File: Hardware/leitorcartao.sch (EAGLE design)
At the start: 160 parts, among them IC1 TL084, IC2 TL084, Q1 DMN3404, Q4 BC847ALT1SMD, Q5 BC847ALT1SMD, Q6 BC847ALT1SMD, Q7 BC847ALT1SMD, Q8 MMBT4403, Q9 MMBT4401, U1 SAMD20E14A-AUT, U3 TLV1117-50CDCYR, U4 MFRC52202HN1, U5 LP2985-33DBVR, X1 MIFARE, X3 ANTENA, Y1 27.12MHz

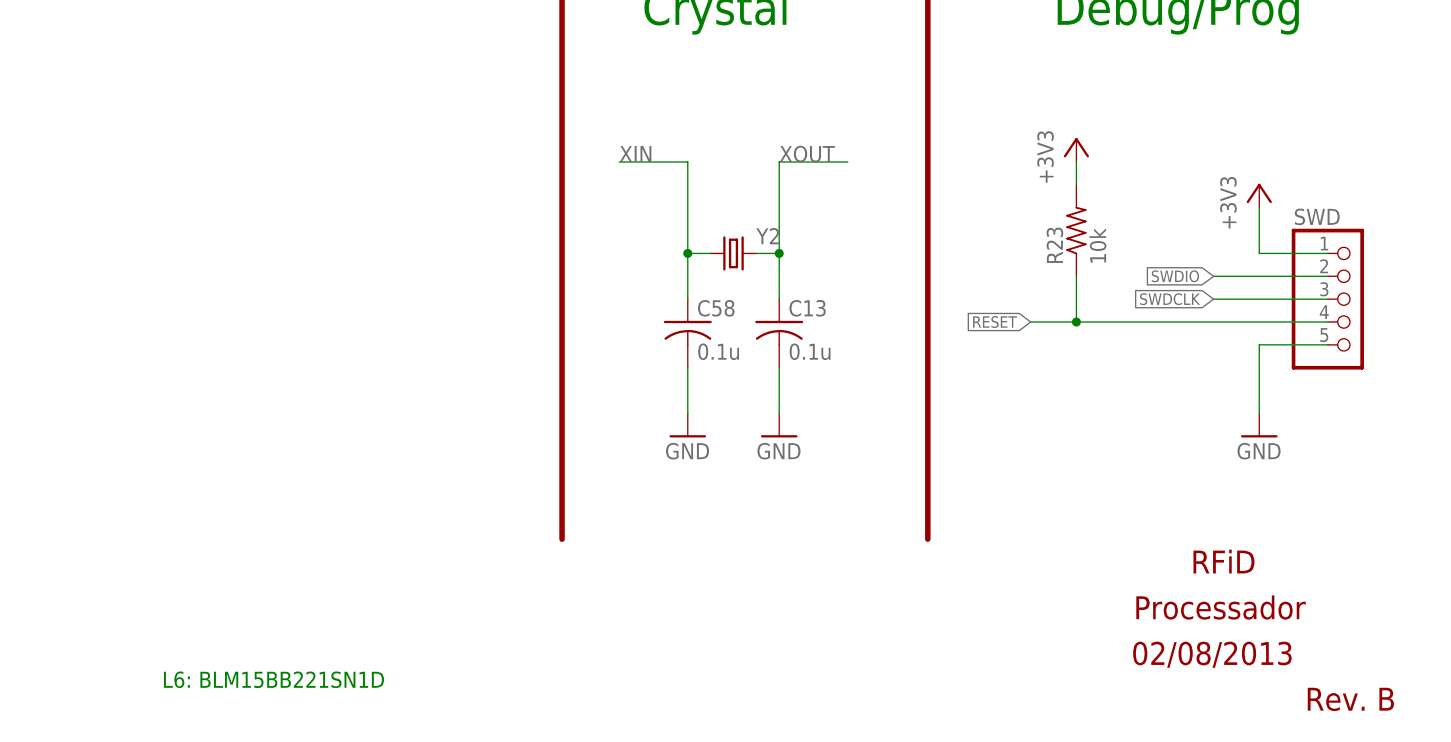
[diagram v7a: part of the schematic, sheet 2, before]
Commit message: Inícios dos trabalhos na BOM do leitor de parede.
Otimização de componentes sendo realizada em conjunto com a elaboração da BOM.
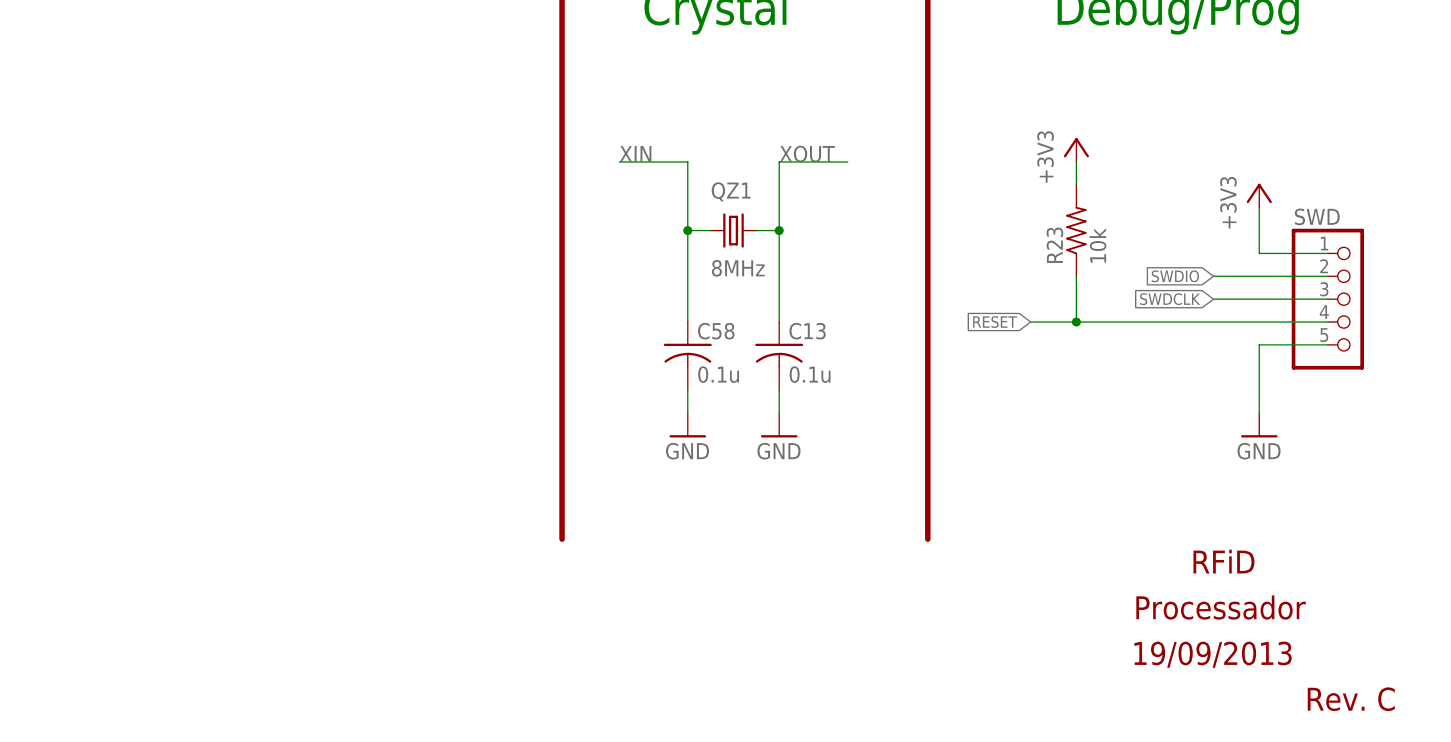
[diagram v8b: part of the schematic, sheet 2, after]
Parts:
- removed Y1: 27.12MHz, ACESSO:CRISTALSMALL(3.2X2.5MM)
- removed Y2: (no value), RFiD:CRYSTALHC49S
- added QZ1: 8MHz, RFiD:CRYSTALHC49S
- added QZ2: 27.12MHz, RFiD:CRISTAL
- BZ1: CUSTOMERPN (none) -> BUZ-REP; CUSTOMER_PN BUZZER -> (none); PN1 (none) -> PS1240P02BT
- C1: CUSTOMERPN (none) -> C/10u/36V/C08; CUSTOMER_PN C/10u/36V/C12 -> (none); PASSIVO (none) -> Sim
- C10, C11, C17, C2, C3, C32, C33, C41: CUSTOMERPN (none) -> C/0.1u/16V/A04; CUSTOMER_PN C/0.1u/16V/C04 -> (none); PASSIVO (none) -> Sim; PN1 (none) -> CL05B104KO5NNNC
- C12, C15, C55, C56: PASSIVO (none) -> Sim
- C13, C42, C58: CUSTOMERPN (none) -> C/0.1u/16V/A04; CUSTOMER_PN C/10u/16V/C08 -> (none); PASSIVO (none) -> Sim; PN1 (none) -> CL05B104KO5NNNC
- C14, C25, C26, C27, C28, C29, C44, C45, C47, C48, C50, C51: CUSTOMER_PN C/1n/100V/C04 -> (none); PASSIVO (none) -> Sim
- C16, C18, C20, C21, C22, C23: CUSTOMER_PN C/2.2n/100V/D04 -> (none); PASSIVO (none) -> Sim
- C19, C46, C49: CUSTOMERPN (none) -> C/0.1u/16V/A04; CUSTOMER_PN C/1n/100V/C04 -> (none); PASSIVO (none) -> Sim; PN1 (none) -> CL05B104KO5NNNC
- C24: value F:C:100p -> F:P:100p; CUSTOMER_PN C/1n/100V/C04 -> (none); PASSIVO (none) -> Sim
- C30, C31: CUSTOMERPN (none) -> C/100p/50V/D04; CUSTOMER_PN C/100p/50V/D04 -> (none); PASSIVO (none) -> Sim
- C34, C35: CUSTOMERPN (none) -> C/120p/50V/D04; CUSTOMER_PN C/120p/50V/D04 -> (none); PASSIVO (none) -> Sim
- C36, C37, C5, C9: CUSTOMERPN (none) -> C/18p/16V/C04; CUSTOMER_PN C/18p/16V/C04 -> (none); PASSIVO (none) -> Sim
- C38, C39: CUSTOMERPN (none) -> C/56p/50V/D04; CUSTOMER_PN C/56p/50V/D04 -> (none); PASSIVO (none) -> Sim
- C4: CUSTOMERPN (none) -> C/10u/16V/C08; CUSTOMER_PN C/10u/16V/C12 -> (none); PASSIVO (none) -> Sim
- C40: CUSTOMERPN (none) -> C/1n/100V/D04; CUSTOMER_PN C/1n/100V/D04 -> (none); PASSIVO (none) -> Sim
- C43, C54, C59, C60: CUSTOMERPN (none) -> C/0.1u/16V/A04; PASSIVO (none) -> Sim; PN1 (none) -> CL05B104KO5NNNC
- C52, C53: CUSTOMERPN (none) -> C/0.1u/16V/A04; CUSTOMER_PN C/2.2n/100V/D04 -> (none); PASSIVO (none) -> Sim; PN1 (none) -> CL05B104KO5NNNC
- C57: CUSTOMER_PN C/0.1u/50V/C04 -> (none); PASSIVO (none) -> Sim
- C6: CUSTOMERPN (none) -> C/10u/36V/C06; CUSTOMER_PN C/10u/36V/C12 -> (none); PASSIVO (none) -> Sim
- C7: CUSTOMERPN (none) -> C/10u/16V/C06; CUSTOMER_PN C/10u/16V/C12 -> (none); PASSIVO (none) -> Sim
- C8: CUSTOMERPN (none) -> C/1m/16V/PTH; CUSTOMER_PN C/ENTRADA -> (none); PASSIVO (none) -> Sim; PN1 (none) -> ESK108M016AH2AA
- CARDPRS, D0/TX/CLK, D1/DATA, GND, LED-IN, MODE, VCC: CUSTOMERPN (none) -> DNP; CUSTOMER_PN - -> (none)
- D1, D3: CUSTOMERPN (none) -> D/BYG20J; PASSIVO (none) -> Sim; PN1 (none) -> BYG20J
- D2: CUSTOMERPN (none) -> TVS/14V/SMA; CUSTOMER_PN D/TVS/SMA -> (none); PASSIVO (none) -> Sim; PN1 (none) -> SMAJ14A
- D5, D6: CUSTOMERPN (none) -> D/BAT54S; CUSTOMER_PN D/BAT54S -> (none); PASSIVO (none) -> Sim
- IC1, IC2: CUSTOMERPN (none) -> IC/TL084/TSSOP14; PN1 (none) -> TL084CPT
- L1, L3: CUSTOMERPN (none) -> L/22n/0.2A/04; CUSTOMER_PN L/22n/0.2A/04 -> (none); PASSIVO (none) -> Sim
- L4, L5: CUSTOMERPN (none) -> L/1u/0.5A/06; CUSTOMER_PN L/1u/0.5A/06 -> (none); PASSIVO (none) -> Sim
- LED1: CUSTOMERPN (none) -> LED/RG/3MM; PN1 (none) -> LTL1BEKVJNN
- Q1: CUSTOMERPN (none) -> Q/DMN3404/SOT23; PN1 (none) -> DMN3404L-7
- Q4, Q5, Q6, Q7: value BC847ALT1SMD -> MMBT4401; device RFiD:BC847ALT1SMD -> RFiD:MMBT4401; CUSTOMERPN (none) -> Q/MMBT4401/SOT23; CUSTOMER_PN Q/BC847A -> (none); PN1 (none) -> MMBT4403LT3G
- Q8: CUSTOMERPN (none) -> Q/MMBT4403/SOT23; PN1 (none) -> MMBT4403LT3G
- Q9: CUSTOMERPN (none) -> Q/MMBT4401/SOT23; PN1 (none) -> MMBT4401LT3G
- R1, R2: CUSTOMERPN (none) -> R/4.7k/5%/04; CUSTOMER_PN R/4.7k/5%/04 -> (none); PASSIVO (none) -> Sim
- R10, R11, R12, R13, R14, R15, R4, R7, R9: CUSTOMER_PN R/1M/5%/04 -> (none); PASSIVO (none) -> Sim
- R16, R17, R18, R19, R21, R22, R45, R48, R51, R52, R53, R54, R55, R56: CUSTOMER_PN R/1k/5%/04 -> (none); PASSIVO (none) -> Sim
- R20: value C:P:270k -> F:P:270k; CUSTOMER_PN R/1k/5%/04 -> (none)
- R23: device RFiD:R-US_R0402 -> RFiD:R-US_R0603; PASSIVO (none) -> Sim
- R24, R25: CUSTOMER_PN R/3.3/5%/04 -> (none); PASSIVO (none) -> Sim
- R26, R3, R32, R33, R34, R43: CUSTOMERPN (none) -> R/2.2k/5%/04; CUSTOMER_PN R/2.2k/5%/04 -> (none); PASSIVO (none) -> Sim
- R27, R29, R30, R31, R44, R49, R5: CUSTOMERPN (none) -> R/1k/5%/04; CUSTOMER_PN R/1k/5%/04 -> (none); PASSIVO (none) -> Sim
- R28, R39, R40: CUSTOMERPN (none) -> R/100k/5%/06; CUSTOMER_PN R/100k/5%/04 -> (none); PASSIVO (none) -> Sim
- R35, R36, R37: CUSTOMERPN (none) -> R/100/5%/04; CUSTOMER_PN R/100/5%/04 -> (none); PASSIVO (none) -> Sim
- R38: CUSTOMER_PN R/10k/5%/04 -> (none); PASSIVO (none) -> Sim
- R41, R42: CUSTOMER_PN R/180/5%/04 -> (none); PASSIVO (none) -> Sim
- R46, R47: CUSTOMER_PN R/39/5%/04 -> (none); PASSIVO (none) -> Sim
- R50, R8: device RFiD:R-US_R0402 -> RFiD:R-US_R0603; CUSTOMERPN (none) -> R/100k/5%/06; CUSTOMER_PN R/1M/5%/04 -> (none); PASSIVO (none) -> Sim
- R57, R58: CUSTOMERPN (none) -> R/470/5%/04; PASSIVO (none) -> Sim
- R59, R60: CUSTOMERPN (none) -> R/12k/5%/04; CUSTOMER_PN R/1k/5%/04 -> (none); PASSIVO (none) -> Sim
- R6: CUSTOMERPN (none) -> R/1M/5%/04; CUSTOMER_PN R/1M/5%/04 -> (none); PASSIVO (none) -> Sim
- R61: CUSTOMERPN (none) -> R/5.1k/5%/04; CUSTOMER_PN R/1k/5%/04 -> (none); PASSIVO (none) -> Sim
- R62, R63: CUSTOMERPN (none) -> R/0/0%/04; CUSTOMER_PN R/1M/5%/04 -> (none); PASSIVO (none) -> Sim
- R64: device RFiD:R-US_R0603 -> RFiD:R-US_R0402; CUSTOMERPN (none) -> R/0/0%/04; CUSTOMER_PN R/1M/5%/04 -> (none); PASSIVO (none) -> Sim
- SWD, X1, X3: CUSTOMERPN (none) -> DNP
- U1: CUSTOMERPN (none) -> IC/SAMD20/TQ32; PN1 (none) -> SAMD20E14A-AUT
- U3: CUSTOMERPN (none) -> IC/5VREG; CUSTOMER_PN IC/5VREG -> (none); PN1 (none) -> TLV1117-50CDCYR
- U4: CUSTOMERPN (none) -> IC/MFRC52202; CUSTOMER_PN IC/MFRC52202 -> (none); PN1 (none) -> MFRC52202HN1,151
- U5: CUSTOMERPN (none) -> IC/3V3REG; PN1 (none) -> LP2985-33DBVR
- renumbered LED2 to LED1, SG1 to BZ1
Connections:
- net GND: now also QZ2.GND@1, QZ2.GND@2; no longer Y1.GND@1, Y1.GND@2
- net N$3: now also QZ2.2; no longer Y1.2
- net N$5: now also QZ2.1; no longer Y1.1
- net XIN: now also QZ1.1; no longer Y2.1
- net XOUT: now also QZ1.2; no longer Y2.2
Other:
- note added: "19/09/2013"
- note added: "Rev. C"
- note removed: "02/08/2013"
- note removed: "L6: BLM15BB221SN1D"
- note removed: "Rev. B"
- moved on the sheet: C13, C58
